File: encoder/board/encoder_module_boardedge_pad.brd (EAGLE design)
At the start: 11 x 13 mm, 5 parts

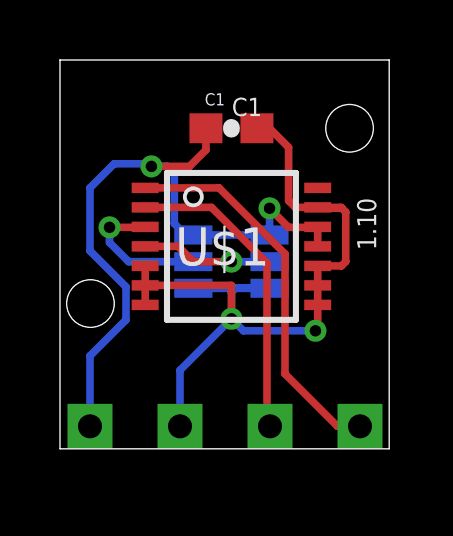
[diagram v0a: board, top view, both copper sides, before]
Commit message: Fixing small things preparing for panelization
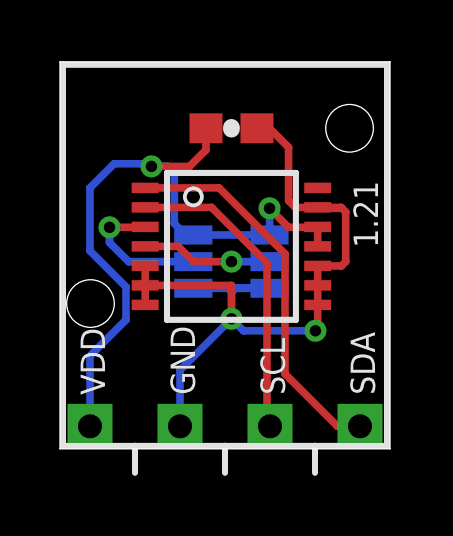
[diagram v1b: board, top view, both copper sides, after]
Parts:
- C1: value 10 uF -> 10uF
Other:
- board size 11 x 13 mm -> 11 x 12.9 mm
- board text added: "1.21"
- board text removed: "1.10"
- board text removed: "C1"
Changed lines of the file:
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@@
 <layer number="14" name="Route14" color="1" fill="6" visible="no" active="no"/>
 <layer number="15" name="Route15" color="4" fill="6" visible="no" active="no"/>
-<layer number="16" name="Bottom" color="1" fill="1" visible="yes" active="yes"/>
+<layer number="16" name="Bottom" color="1" fill="1" visible="no" active="yes"/>
 <layer number="17" name="Pads" color="2" fill="1" visible="yes" active="yes"/>
 <layer number="18" name="Vias" color="2" fill="1" visible="yes" active="yes"/>
 <layer number="19" name="Unrouted" color="1" fill="1" visible="yes" active="yes"/>
 <layer number="20" name="Dimension" color="15" fill="1" visible="yes" active="yes"/>
-<layer number="21" name="tPlace" color="15" fill="1" visible="no" active="yes"/>
+<layer number="21" name="tPlace" color="15" fill="1" visible="yes" active="yes"/>
 <layer number="22" name="bPlace" color="7" fill="1" visible="no" active="yes"/>
-<layer number="23" name="tOrigins" color="15" fill="1" visible="no" active="yes"/>
+<layer number="23" name="tOrigins" color="15" fill="1" visible="yes" active="yes"/>
 <layer number="24" name="bOrigins" color="15" fill="1" visible="no" active="yes"/>
-<layer number="25" name="tNames" color="7" fill="1" visible="no" active="yes"/>
+<layer number="25" name="tNames" color="7" fill="1" visible="yes" active="yes"/>
 <layer number="26" name="bNames" color="7" fill="1" visible="no" active="yes"/>
-<layer number="27" name="tValues" color="7" fill="1" visible="no" active="yes"/>
+<layer number="27" name="tValues" color="7" fill="1" visible="yes" active="yes"/>
 <layer number="28" name="bValues" color="7" fill="1" visible="no" active="yes"/>
-<layer number="29" name="tStop" color="7" fill="3" visible="no" active="yes"/>
+<layer number="29" name="tStop" color="7" fill="3" visible="yes" active="yes"/>
 <layer number="30" name="bStop" color="7" fill="6" visible="no" active="yes"/>
 <layer number="31" name="tCream" color="7" fill="4" visible="no" active="yes"/>
@@
 <layer number="37" name="tTest" color="7" fill="1" visible="no" active="yes"/>
 <layer number="38" name="bTest" color="7" fill="1" visible="no" active="yes"/>
-<layer number="39" name="tKeepout" color="4" fill="11" visible="no" active="yes"/>
+<layer number="39" name="tKeepout" color="4" fill="11" visible="yes" active="yes"/>
 <layer number="40" name="bKeepout" color="1" fill="11" visible="no" active="yes"/>
 <layer number="41" name="tRestrict" color="4" fill="10" visible="no" active="yes"/>
@@
 <layer number="46" name="Milling" color="3" fill="1" visible="no" active="yes"/>
 <layer number="47" name="Measures" color="7" fill="1" visible="no" active="yes"/>
-<layer number="48" name="Document" color="7" fill="1" visible="no" active="yes"/>
+<layer number="48" name="Document" color="7" fill="1" visible="yes" active="yes"/>
 <layer number="49" name="Reference" color="7" fill="1" visible="no" active="yes"/>
 <layer number="50" name="dxf" color="7" fill="1" visible="no" active="no"/>
@@
 <layer number="144" name="Drill_legend" color="7" fill="1" visible="no" active="yes"/>
 <layer number="151" name="HeatSink" color="7" fill="1" visible="no" active="yes"/>
-<layer number="199" name="Contour" color="7" fill="1" visible="yes" active="yes"/>
+<layer number="199" name="Contour" color="7" fill="1" visible="no" active="yes"/>
 <layer number="200" name="200bmp" color="1" fill="10" visible="no" active="yes"/>
 <layer number="201" name="201bmp" color="2" fill="10" visible="no" active="yes"/>
@@
 <board>
 <plain>
-<wire x1="0" y1="-3.7" x2="10.973" y2="-3.7" width="0" layer="20"/>
-<wire x1="10.973" y1="-3.7" x2="10.973" y2="9.261" width="0" layer="20"/>
-<wire x1="10.973" y1="9.261" x2="0" y2="9.261" width="0" layer="20"/>
-<wire x1="0" y1="9.261" x2="0" y2="-3.7" width="0" layer="20"/>
-<text x="8.636" y="3.937" size="0.6096" layer="22" rot="MR0">1</text>
-<text x="9.144" y="2.921" size="0.6096" layer="22" rot="MR0">A1</text>
-<text x="8.763" y="1.778" size="0.6096" layer="22" rot="MR0">0</text>
-<text x="3.048" y="4.064" size="0.6096" layer="22" rot="MR0">1</text>
-<text x="3.048" y="1.905" size="0.6096" layer="22" rot="MR0">0</text>
-<text x="3.175" y="3.048" size="0.6096" layer="22" rot="MR0">A2</text>
-<text x="2.032" y="6.35" size="0.6096" layer="22" rot="MR0">VDD</text>
-<text x="2.032" y="7.239" size="0.6096" layer="22" rot="MR0">GND</text>
-<text x="2.032" y="4.318" size="0.6096" layer="22" rot="MR0">SCL</text>
-<text x="2.032" y="5.334" size="0.6096" layer="22" rot="MR0">SDA</text>
-<text x="6.731" y="8.001" size="0.6096" layer="21" rot="R180">C1</text>
+<wire x1="0" y1="-3.7" x2="11" y2="-3.7" width="0" layer="20"/>
+<wire x1="11" y1="-3.7" x2="11" y2="9.2" width="0" layer="20"/>
+<wire x1="11" y1="9.2" x2="0" y2="9.2" width="0" layer="20"/>
+<wire x1="0" y1="9.2" x2="0" y2="-3.7" width="0" layer="20"/>
+<text x="8.8" y="3.1" size="0.8128" layer="22" ratio="20" rot="MR0">1</text>
+<text x="9.6" y="2.1" size="0.8128" layer="22" ratio="20" rot="MR0">A1</text>
+<text x="8.8" y="1" size="0.8128" layer="22" ratio="20" rot="MR0">0</text>
+<text x="3" y="3.2" size="0.8128" layer="22" ratio="20" rot="MR0">1</text>
+<text x="3.1" y="1" size="0.8128" layer="22" ratio="20" rot="MR0">0</text>
+<text x="3.1" y="2.1" size="0.8128" layer="22" ratio="20" rot="MR0">A2</text>
+<text x="1.5" y="-1.9" size="0.8128" layer="21" ratio="20" rot="R90">VDD</text>
+<text x="4.5" y="-1.9" size="0.8128" layer="21" ratio="20" rot="R90">GND</text>
+<text x="7.5" y="-1.9" size="0.8128" layer="21" ratio="20" rot="R90">SCL</text>
+<text x="10.5" y="-1.9" size="0.8128" layer="21" ratio="20" rot="R90">SDA</text>
 <hole x="1.016" y="1.143" drill="1.5875"/>
 <hole x="9.652" y="6.985" drill="1.5875"/>
-<text x="10.541" y="2.921" size="0.635" layer="21" rot="R90">1.10</text>
+<text x="10.6" y="3" size="0.8128" layer="21" ratio="20" rot="R90">1.21</text>
+<wire x1="0.1" y1="-3.6" x2="0.1" y2="9.1" width="0.2" layer="21"/>
+<wire x1="0.1" y1="9.1" x2="10.9" y2="9.1" width="0.2" layer="21"/>
+<wire x1="10.9" y1="9.1" x2="10.9" y2="-3.6" width="0.2" layer="21"/>
+<wire x1="10.9" y1="-3.6" x2="8.5" y2="-3.6" width="0.2" layer="21"/>
+<wire x1="8.5" y1="-3.6" x2="5.5" y2="-3.6" width="0.2" layer="21"/>
+<wire x1="5.5" y1="-3.6" x2="2.5" y2="-3.6" width="0.2" layer="21"/>
+<wire x1="2.5" y1="-3.6" x2="0.1" y2="-3.6" width="0.2" layer="21"/>
+<wire x1="2.5" y1="-4.5" x2="2.5" y2="-3.6" width="0.2" layer="21"/>
+<wire x1="5.5" y1="-4.5" x2="5.5" y2="-3.6" width="0.2" layer="21"/>
+<wire x1="8.5" y1="-4.5" x2="8.5" y2="-3.6" width="0.2" layer="21"/>
+<wire x1="0.1" y1="-3.6" x2="0.1" y2="9.1" width="0.2" layer="22"/>
+<wire x1="0.1" y1="9.1" x2="10.9" y2="9.1" width="0.2" layer="22"/>
+<wire x1="10.9" y1="9.1" x2="10.9" y2="-3.6" width="0.2" layer="22"/>
+<wire x1="10.9" y1="-3.6" x2="8.5" y2="-3.6" width="0.2" layer="22"/>
+<wire x1="8.5" y1="-3.6" x2="5.5" y2="-3.6" width="0.2" layer="22"/>
+<wire x1="5.5" y1="-3.6" x2="2.5" y2="-3.6" width="0.2" layer="22"/>
+<wire x1="2.5" y1="-3.6" x2="0.1" y2="-3.6" width="0.2" layer="22"/>
+<wire x1="2.5" y1="-4.5" x2="2.5" y2="-3.6" width="0.2" layer="22"/>
+<wire x1="5.5" y1="-4.5" x2="5.5" y2="-3.6" width="0.2" layer="22"/>
+<wire x1="8.5" y1="-4.5" x2="8.5" y2="-3.6" width="0.2" layer="22"/>
 </plain>
 <attributes>
@@
 </autorouter>
 <elements>
-<element name="U$1" library="austriamicrosystems" package="TSSOP14" value="AS5048B" x="5.715" y="3.048" smashed="yes">
-<attribute name="NAME" x="6.985" y="3.683" size="1.27" layer="25" rot="R180"/>
-<attribute name="VALUE" x="14.478" y="5.969" size="1.27" layer="27"/>
+<element name="U$1" library="austriamicrosystems" package="TSSOP14" value="AS5048B" x="5.715" y="3.048" smashed="yes"/>
+<element name="C1" library="SparkFun" package="0603-CAP" value="10uF" x="5.715" y="6.985" smashed="yes">
+<attribute name="VALUE" x="1" y="6.5" size="0.8128" layer="27" font="vector" ratio="20"/>
 </element>
-<element name="C1" library="SparkFun" package="0603-CAP" value="10 uF" x="5.715" y="6.985"/>
-<element name="SJ5" library="SparkFun" package="SJ_3" value="" x="6.985" y="2.54" rot="MR90"/>
-<element name="SJ6" library="SparkFun" package="SJ_3" value="" x="4.445" y="2.54" rot="MR270"/>
-<element name="JP1" library="modular_robotics" package="1X4_3MM_BOARDEDGE_VERT" value="" x="5.5" y="-3.7"/>
+<element name="SJ5" library="SparkFun" package="SJ_3" value="" x="6.985" y="2.54" smashed="yes" rot="MR90">
+<attribute name="VALUE" x="6.985" y="2.4399" size="0.02" layer="28" rot="MR90"/>
+<attribute name="VALUE" x="5.08" y="1.27" size="0.4064" layer="28" rot="MR90"/>
+</element>
+<element name="SJ6" library="SparkFun" package="SJ_3" value="" x="4.445" y="2.54" smashed="yes" rot="MR270">
+<attribute name="VALUE" x="4.445" y="2.6401" size="0.02" layer="28" rot="MR270"/>
+<attribute name="VALUE" x="6.35" y="3.81" size="0.4064" layer="28" rot="MR270"/>
+</element>
+<element name="JP1" library="modular_robotics" package="1X4_3MM_BOARDEDGE_VERT" value="" x="5.5" y="-3.7" smashed="yes"/>
 </elements>
 <signals>

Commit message: Got rid of holes in 20 csp through package. Preparing for job submission pending spacing check.
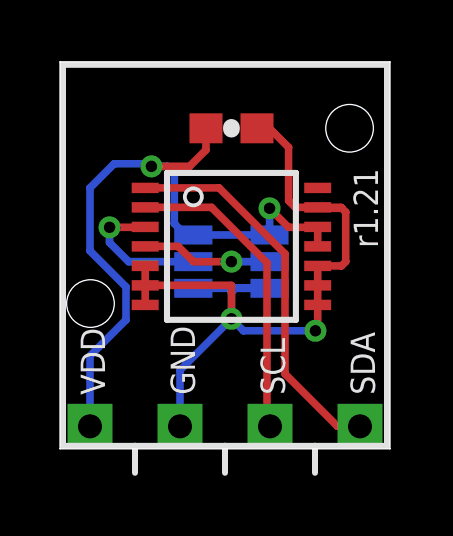
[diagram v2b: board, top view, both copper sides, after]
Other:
- board text added: "r1.21"
- board text removed: "1.21"
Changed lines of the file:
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@@
 <hole x="1.016" y="1.143" drill="1.5875"/>
 <hole x="9.652" y="6.985" drill="1.5875"/>
-<text x="10.6" y="3" size="0.8128" layer="21" ratio="20" rot="R90">1.21</text>
+<text x="10.6" y="3" size="0.8128" layer="21" ratio="20" rot="R90">r1.21</text>
 <wire x1="0.1" y1="-3.6" x2="0.1" y2="9.1" width="0.2" layer="21"/>
 <wire x1="0.1" y1="9.1" x2="10.9" y2="9.1" width="0.2" layer="21"/>
